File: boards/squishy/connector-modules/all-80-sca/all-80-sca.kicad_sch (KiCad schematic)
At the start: 14 parts, among them J1 SCSI PHY Mezz, J2 Conn_02x25_Odd_Even, J3 Conn_01x04, J4 Conn_02x34_Clockwise_Shield, J5 Conn_02x24_Clockwise_Shield, U1 M24C02-RMC

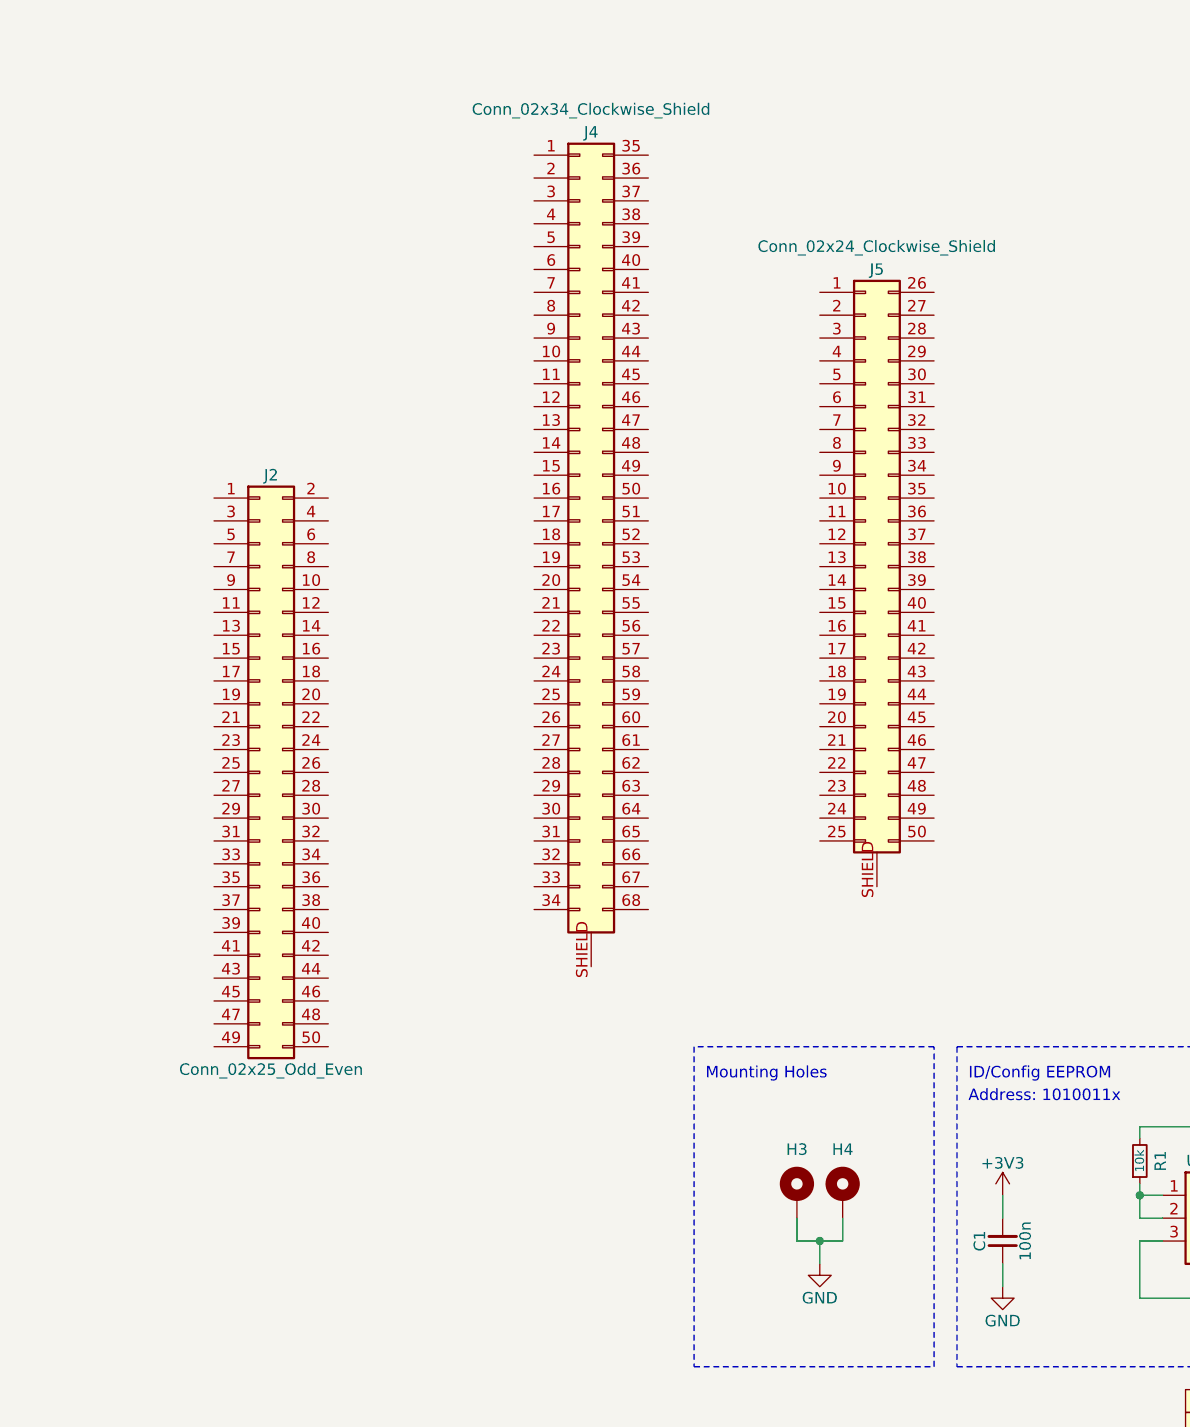
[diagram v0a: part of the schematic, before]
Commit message: squishy: connectors: Removed unneeded connector symbols in the given kicad schematics
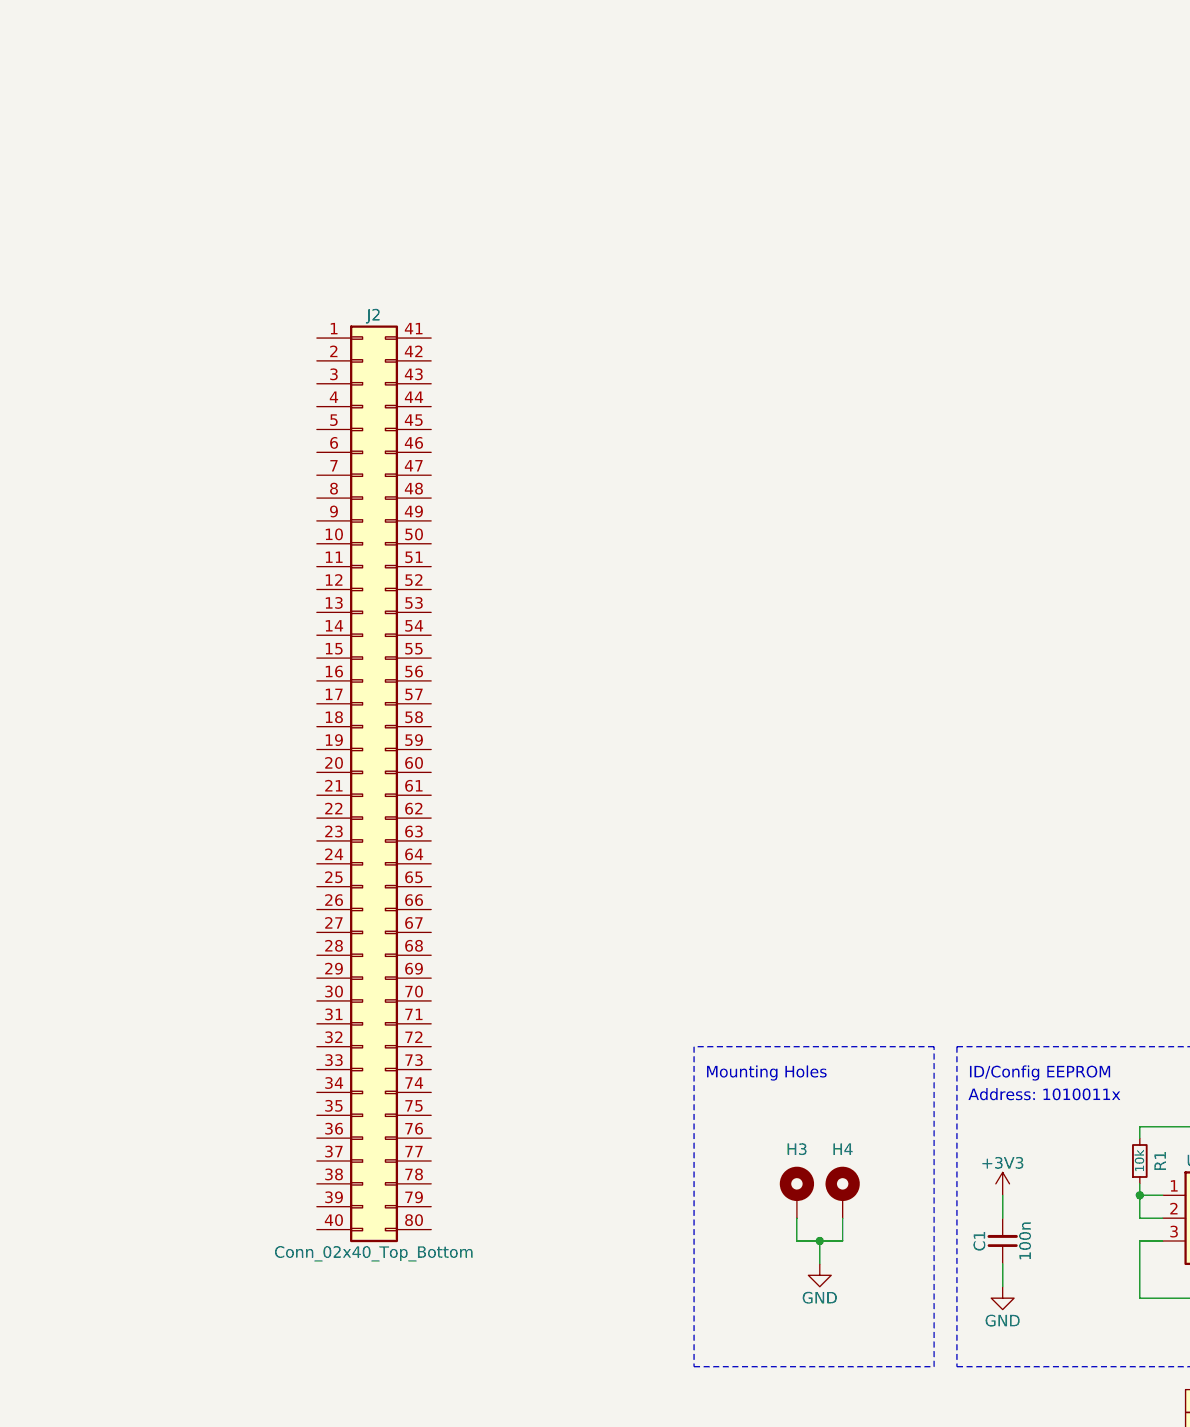
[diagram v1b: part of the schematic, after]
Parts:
- removed J2: Conn_02x25_Odd_Even, Connector_IDC:IDC-Header_2x25_P2.54mm_Horizontal, symbol Connector_Generic:Conn_02x25_Odd_Even
- removed J4: Conn_02x34_Clockwise_Shield, symbol lethalbit-connectors:Conn_02x34_Counter_Clockwise
- removed J5: Conn_02x24_Clockwise_Shield, symbol lethalbit-connectors:Conn_02x25_Counter_Clockwise
- added J2: Conn_02x40_Top_Bottom, symbol Connector_Generic:Conn_02x40_Top_Bottom

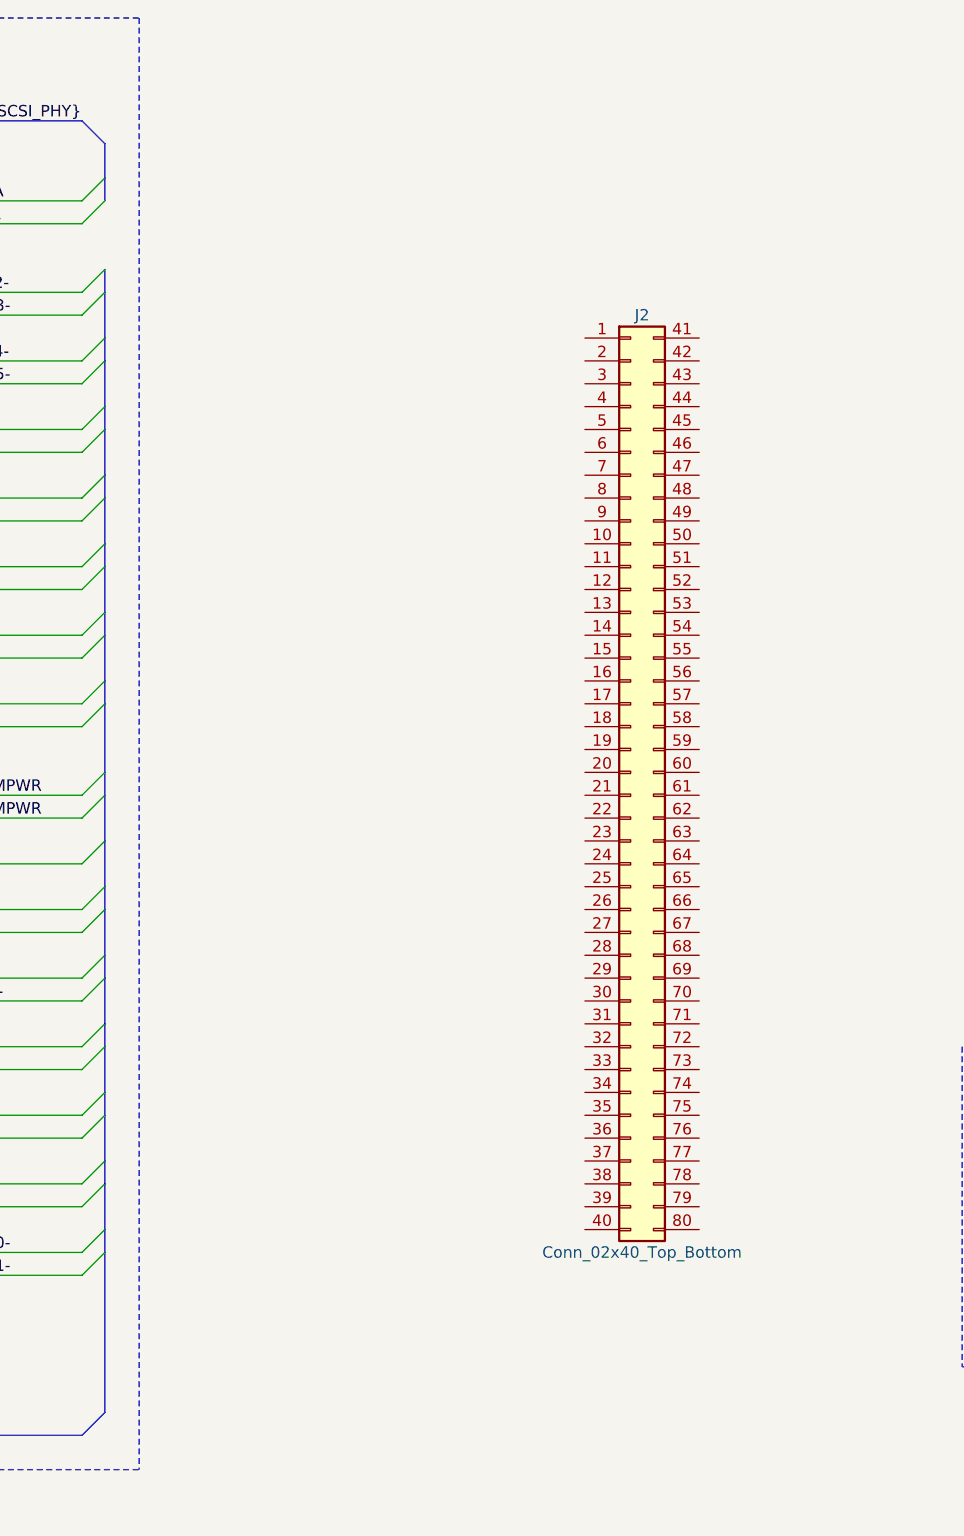
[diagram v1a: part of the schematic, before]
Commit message: squishy: connectors: Cleaned up and unified look/feel of connector schematics
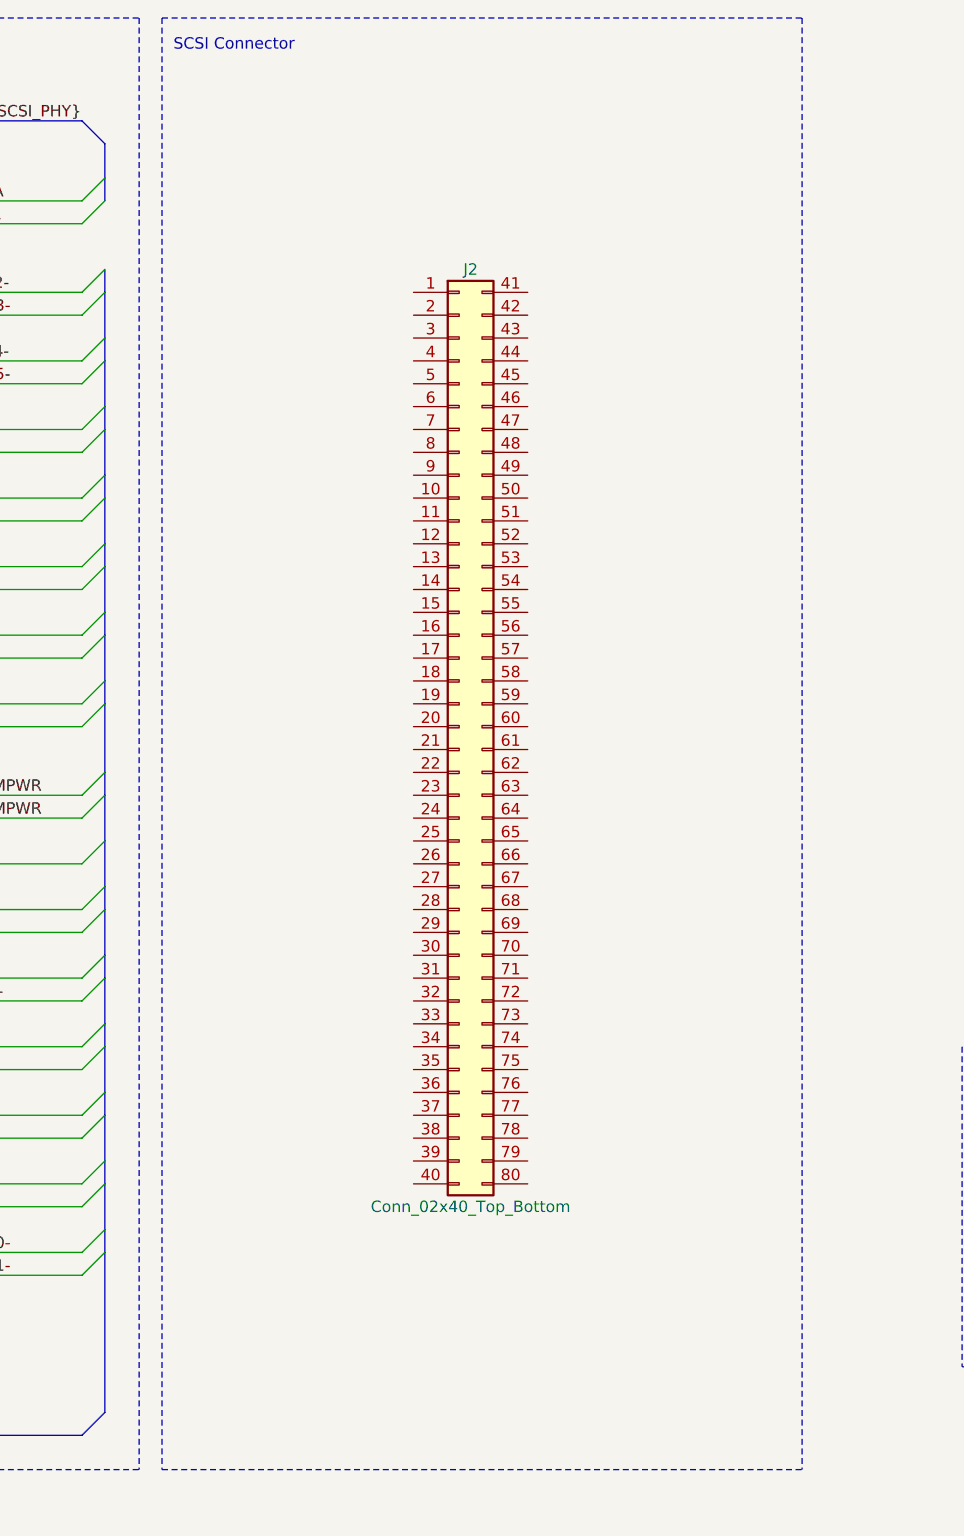
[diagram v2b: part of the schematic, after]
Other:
- note added: "SCSI Connector"
- moved on the sheet: J2
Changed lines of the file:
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@@
 		)
 	)
+	(polyline
+		(pts
+			(xy 87.63 13.97) (xy 87.63 175.26)
+		)
+		(stroke
+			(width 0)
+			(type dash)
+		)
+	)
 	(wire
 		(pts
@@
 		)
 	)
+	(polyline
+		(pts
+			(xy 158.75 13.97) (xy 158.75 175.26)
+		)
+		(stroke
+			(width 0)
+			(type dash)
+		)
+	)
 	(wire
 		(pts
@@
 		)
 	)
+	(polyline
+		(pts
+			(xy 87.63 13.97) (xy 158.75 13.97)
+		)
+		(stroke
+			(width 0)
+			(type dash)
+		)
+	)
 	(wire
 		(pts
@@
 		)
 	)
+	(polyline
+		(pts
+			(xy 87.63 175.26) (xy 158.75 175.26)
+		)
+		(stroke
+			(width 0)
+			(type dash)
+		)
+	)
 	(bus
 		(pts
@@
 		)
 	)
+	(text "SCSI Connector"
+		(exclude_from_sim no)
+		(at 88.9 17.78 0)
+		(effects
+			(font
+				(size 1.27 1.27)
+			)
+			(justify left bottom)
+		)
+	)
 	(text "Mounting Holes\n"
 		(exclude_from_sim no)
@@
 	(symbol
 		(lib_id "Connector_Generic:Conn_02x40_Top_Bottom")
-		(at 139.7 97.79 0)
+		(at 120.65 92.71 0)
 		(unit 1)
 		(exclude_from_sim no)
@@
 		(dnp no)
 		(property "Reference" "J2"
-			(at 140.97 46.99 0)
+			(at 121.92 41.91 0)
 			(effects
 				(font
@@
 		)
 		(property "Value" "Conn_02x40_Top_Bottom"
-			(at 140.97 151.13 0)
+			(at 121.92 146.05 0)
 			(effects
 				(font
@@
 		)
 		(property "Footprint" ""
-			(at 139.7 97.79 0)
+			(at 120.65 92.71 0)
 			(effects
 				(font
@@
 		)
 		(property "Datasheet" "~"
-			(at 139.7 97.79 0)
+			(at 120.65 92.71 0)
 			(effects
 				(font
@@
 		)
 		(property "Description" "Generic connector, double row, 02x40, top/bottom pin numbering scheme (row 1: 1...pins_per_row, row2: pins_per_row+1 ... num_pins), script generated (kicad-library-utils/schlib/autogen/connector/)"
-			(at 139.7 97.79 0)
+			(at 120.65 92.71 0)
 			(effects
 				(font

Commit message: squishy: connectors: updated schematic title blocks for connectors as appropriate
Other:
- title: Squishy -  ICD 50 -> Squishy -  SCSI SCA-2 80 Connector Module
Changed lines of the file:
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@@
 	(paper "A4")
 	(title_block
-		(title "Squishy -  ICD 50")
-		(date "2024-08-22")
+		(title "Squishy -  SCSI SCA-2 80 Connector Module")
+		(date "2024-09-17")
 		(rev "1")
 		(company "Shrine Maiden Heavy Industries")

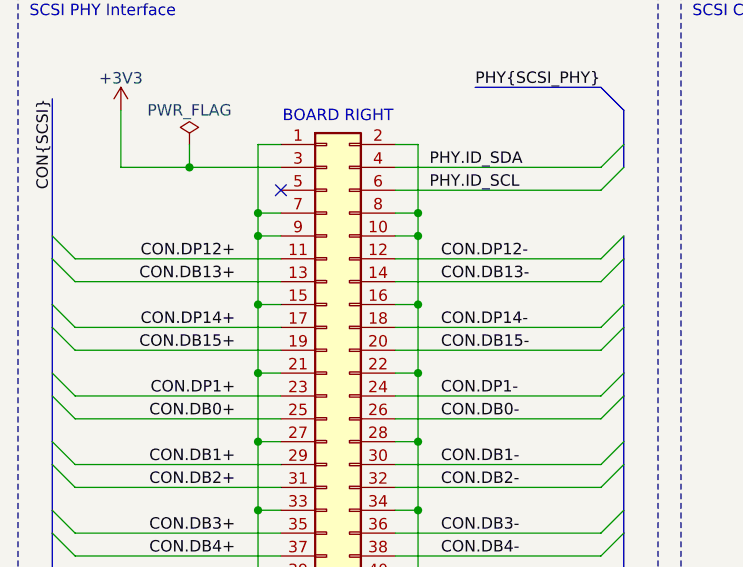
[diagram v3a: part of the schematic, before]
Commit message: squishy: connectors: s/DP12/DB12/g s/DP14/DB14/g
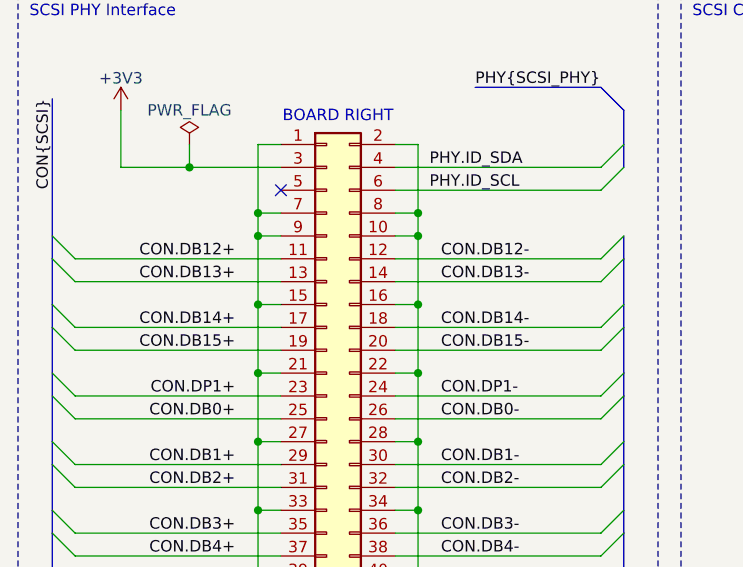
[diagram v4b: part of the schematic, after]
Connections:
- net CON.DP12+ renamed CON.DB12+
- net CON.DP12- renamed CON.DB12-
- net CON.DP14+ renamed CON.DB14+
- net CON.DP14- renamed CON.DB14-
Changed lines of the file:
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@@
 		)
 	)
-	(label "CON.DP14-"
+	(label "CON.DB14-"
 		(at 60.96 52.07 0)
 		(fields_autoplaced yes)
@@
 		)
 	)
-	(label "CON.DP12+"
+	(label "CON.DB12+"
 		(at 38.1 44.45 180)
 		(fields_autoplaced yes)
@@
 		)
 	)
-	(label "CON.DP12-"
+	(label "CON.DB12-"
 		(at 60.96 44.45 0)
 		(fields_autoplaced yes)
@@
 		)
 	)
-	(label "CON.DP14+"
+	(label "CON.DB14+"
 		(at 38.1 52.07 180)
 		(fields_autoplaced yes)
